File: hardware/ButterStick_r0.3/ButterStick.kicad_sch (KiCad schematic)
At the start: 7 parts

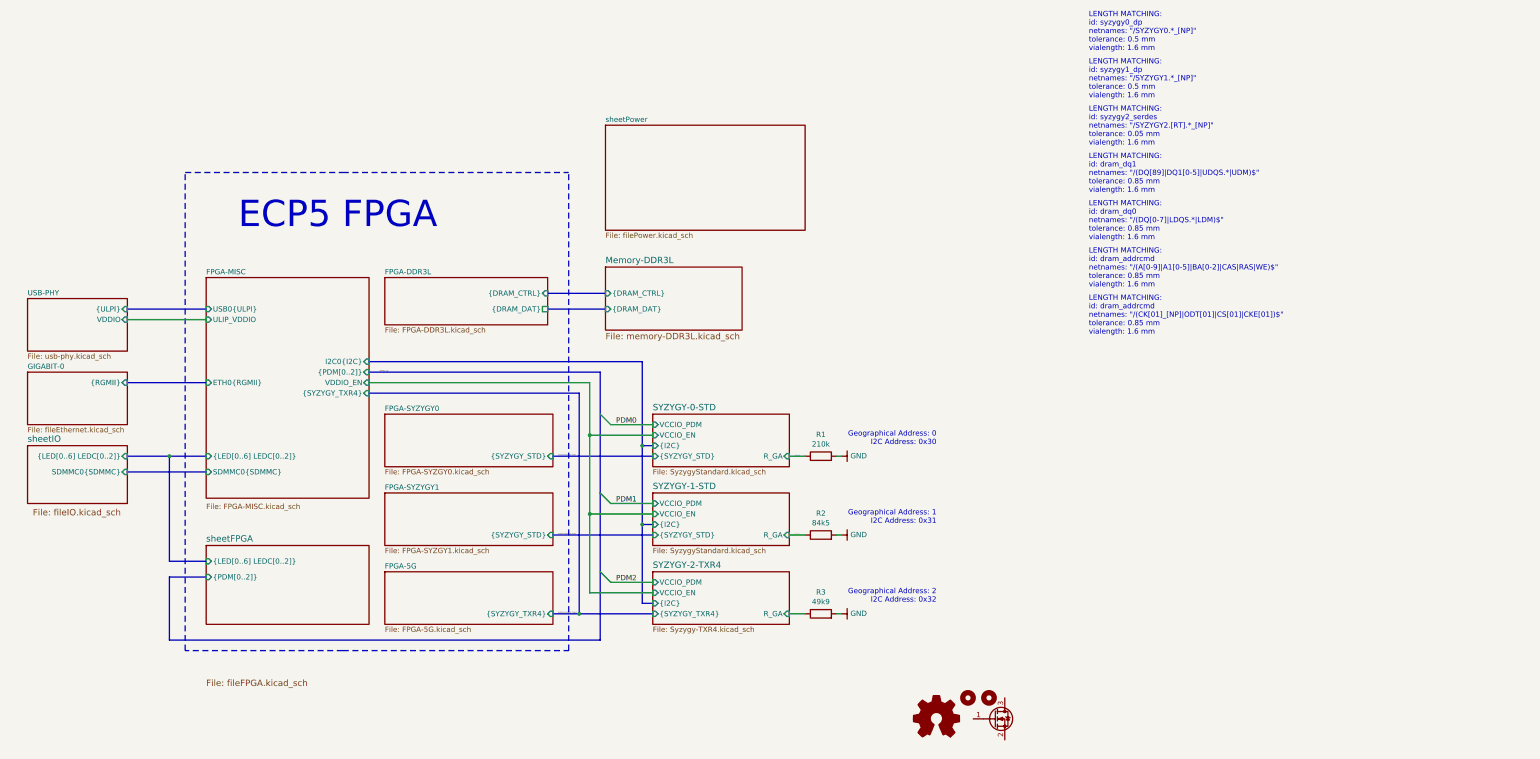
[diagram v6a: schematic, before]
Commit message: hw.r0d3: Fix ULPI VCCIO
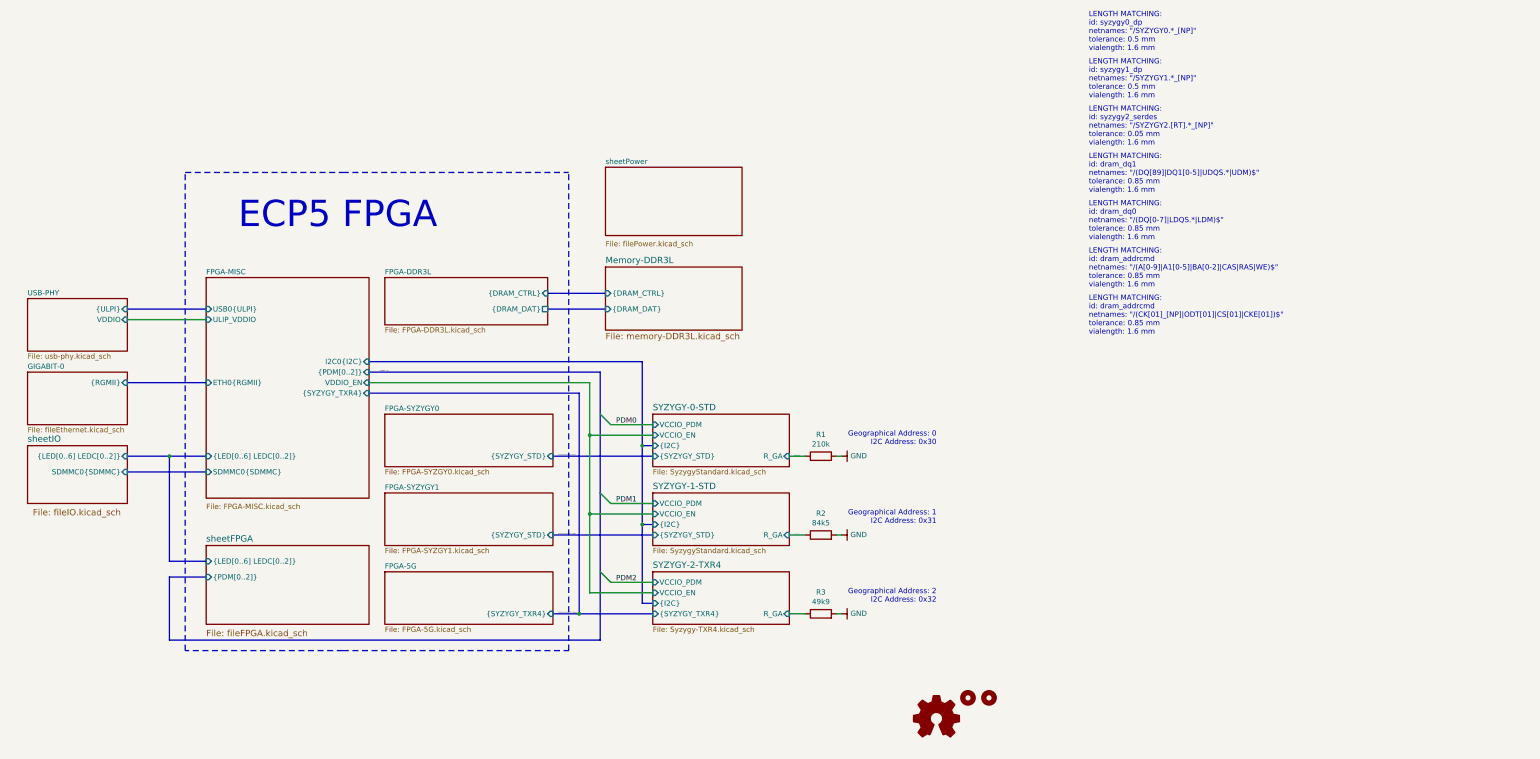
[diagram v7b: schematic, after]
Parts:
- removed LOGO1: Q_NMOS_GSD, gkl_logos:gsd_logo_small, symbol Device:Q_NMOS_GSD
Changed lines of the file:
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@@
-    )
-  )
-  (symbol (lib_id "Device:Q_NMOS_GSD") (at 278.13 173.99 0) (unit 1)
-    (in_bom no) (on_board yes)
-    (property "Reference" "LOGO1" (id 0) (at 283.3371 172.8406 0)
-      (effects (font (size 1.27 1.27)) (justify left) hide)
-    )
-    (property "Value" "Q_NMOS_GSD" (id 1) (at 283.3371 175.1393 0)
-      (effects (font (size 1.27 1.27)) (justify left) hide)
-    )
-    (property "Footprint" "gkl_logos:gsd_logo_small" (id 2) (at 283.21 171.45 0)
-      (effects (font (size 1.27 1.27)) hide)
-    )
-    (property "Datasheet" "~" (id 3) (at 278.13 173.99 0)
-      (effects (font (size 1.27 1.27)) hide)
     )
   )
@@
       (effects (font (size 1.27 1.27)) (justify left))
     )
+    (pin "USB0{ULPI}" input (at 87.63 74.93 180)
+      (effects (font (size 1.27 1.27)) (justify left))
+    )
+    (pin "ETH0{RGMII}" input (at 87.63 92.71 180)
+      (effects (font (size 1.27 1.27)) (justify left))
+    )
+    (pin "ULIP_VDDIO" input (at 87.63 77.47 180)
+      (effects (font (size 1.27 1.27)) (justify left))
+    )
+    (pin "I2C0{I2C}" input (at 127 87.63 0)
+      (effects (font (size 1.27 1.27)) (justify right))
+    )
+    (pin "VDDIO_EN" input (at 127 92.71 0)
+      (effects (font (size 1.27 1.27)) (justify right))
+    )
+    (pin "SDMMC0{SDMMC}" input (at 87.63 114.3 180)
+      (effects (font (size 1.27 1.27)) (justify left))
+    )
+    (pin "{PDM[0..2]}" input (at 127 90.17 0)
+      (effects (font (size 1.27 1.27)) (justify right))
+    )
     (pin "{SYZYGY_TXR4}" input (at 127 95.25 0)
-      (effects (font (size 1.27 1.27)) (justify right))
-    )
-    (pin "USB0{ULPI}" input (at 87.63 74.93 180)
-      (effects (font (size 1.27 1.27)) (justify left))
-    )
-    (pin "ETH0{RGMII}" input (at 87.63 92.71 180)
-      (effects (font (size 1.27 1.27)) (justify left))
-    )
-    (pin "ULIP_VDDIO" input (at 87.63 77.47 180)
-      (effects (font (size 1.27 1.27)) (justify left))
-    )
-    (pin "I2C0{I2C}" input (at 127 87.63 0)
-      (effects (font (size 1.27 1.27)) (justify right))
-    )
-    (pin "VDDIO_EN" input (at 127 92.71 0)
-      (effects (font (size 1.27 1.27)) (justify right))
-    )
-    (pin "SDMMC0{SDMMC}" input (at 87.63 114.3 180)
-      (effects (font (size 1.27 1.27)) (justify left))
-    )
-    (pin "{PDM[0..2]}" input (at 127 90.17 0)
       (effects (font (size 1.27 1.27)) (justify right))
     )
@@
       (effects (font (size 1.524 1.524)) (justify left bottom))
     )
-    (property "Sheet file" "fileFPGA.kicad_sch" (id 1) (at 87.63 164.4401 0)
+    (property "Sheet file" "fileFPGA.kicad_sch" (id 1) (at 87.63 152.4 0)
       (effects (font (size 1.524 1.524)) (justify left top))
     )
@@
     )
   )
-  (sheet (at 184.15 30.48) (size 48.26 25.4)
-    (stroke (width 0.1524) (type solid) (color 132 0 132 1))
-    (fill (color 255 255 255 1.0000))
-    (property "Sheet name" "sheetPower" (id 0) (at 184.15 29.8445 0)
+  (sheet (at 184.15 40.64) (size 33.02 16.51)
+    (stroke (width 0.1524) (type solid) (color 132 0 132 1))
+    (fill (color 255 255 255 1.0000))
+    (property "Sheet name" "sheetPower" (id 0) (at 184.15 40.0045 0)
       (effects (font (size 1.27 1.27)) (justify left bottom))
     )
-    (property "Sheet file" "filePower.kicad_sch" (id 1) (at 184.15 56.3885 0)
+    (property "Sheet file" "filePower.kicad_sch" (id 1) (at 184.15 58.42 0)
       (effects (font (size 1.27 1.27)) (justify left top))
     )
@@
       (reference "H2") (unit 1)
     )
-    (path "/3c7967e0-8afd-4c24-bec4-4c23a51d103b"
-      (reference "LOGO1") (unit 1)
-    )
     (path "/37f38a3d-d77d-4ab6-a577-52b8d43f83c8"
       (reference "LOGO2") (unit 1)
@@
       (reference "C24") (unit 1)
     )
+    (path "/143efee5-76ce-4cba-84a0-fbafa001f7dd/a608112e-dc76-47e5-a13e-9b9541c47e39"
+      (reference "NT1") (unit 1)
+    )
     (path "/143efee5-76ce-4cba-84a0-fbafa001f7dd/cbc8317b-04cc-4ae1-ac01-5fc4d13ebdd5"
